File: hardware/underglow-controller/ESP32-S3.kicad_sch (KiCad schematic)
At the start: 38 parts, among them J101 CONSOLE, SW101 SW_Push, SW102 SW_Push, U101 ESP32-S3R2, U102 W25Q128JVS, Y101 40MHZ

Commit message: Hardware updates, firmware updates blah blah blah
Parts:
- added C111: 1uF, Capacitor_SMD:C_0402_1005Metric, symbol Device:C_Small
- added C118: 0.1uF, Capacitor_SMD:C_0402_1005Metric, symbol Device:C_Small
- added L103: 2nH, Inductor_SMD:L_0402_1005Metric, symbol Device:L_Small
- C108: value 1uF -> 10nf; MPN CGA2B1X7T0G105M050BC -> (none)
- C109: value 10uF -> 1uF; MPN GRT21BC81A106KE01L -> (none)
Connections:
- net +3V3: now also L103.2; no longer C101.1, C106.1, C110.1, R105.1, U101.2 (VDD3P3), U101.20 (VDD3P3_RTC), U101.29 (VDD_SPI), U101.3 (VDD3P3), U102.8 (VCC)
- net GND: now also C111.2, C118.2
- new net VDD3V3: C118.1, L103.1, U101.2 (VDD3P3), U101.3 (VDD3P3)
- new net VDDRTC: C101.1, U101.20 (VDD3P3_RTC)
- new net VDDSPI: C106.1, C110.1, C111.1, R105.1, U101.29 (VDD_SPI), U102.8 (VCC)
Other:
- moved on the sheet: C101, C102, C103, C104, C105, C106, C107, C108, C109

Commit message: hardware updates
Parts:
- removed AE101: Antenna_Shield, RF_Antenna:Texas_SWRA117D_2.4GHz_Left, symbol Device:Antenna_Shield
- removed J101: CONSOLE, Connector_PinHeader_1.27mm:PinHeader_1x06_P1.27mm_Vertical, symbol Connector_Generic:Conn_01x06
- added ANT101: 47948-0001, ConeCodes:Molex-47948-0001-0-0-0, symbol ConeCodes:47948-0001
- added C119: 2pF, Capacitor_SMD:C_0402_1005Metric, symbol Device:C_Small
- added J101: TC2030-IDC-NL_ESP, Connector:Tag-Connect_TC2030-IDC-FP_2x03_P1.27mm_Vertical, symbol ConeCodes:TC2030-IDC-NL_ESP
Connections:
- net FSPICS1: now also J101.6 (IO0)
- net GND: now also C119.1, J101.4 (GND)
- net RF_ANT: now also C119.2
- net RF_ANT_CHIP: now reaches C116.2, L102.2
- net RF_ANT_CHIP: now also ANT101.2 (FEEDING_PAD)
- net CHIP_PU renamed EN
- net EN: now also J101.1 (EN)
- net U0RXD renamed RXD
- net RXD: now also J101.5 (RX)
- net U0TXD renamed TXD
- net TXD: now also J101.3 (TX)
- no-connect marks 3 -> 6
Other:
- moved on the sheet: C114, C115, C116, L101, L102, TP101, TP102, TP103, TP104

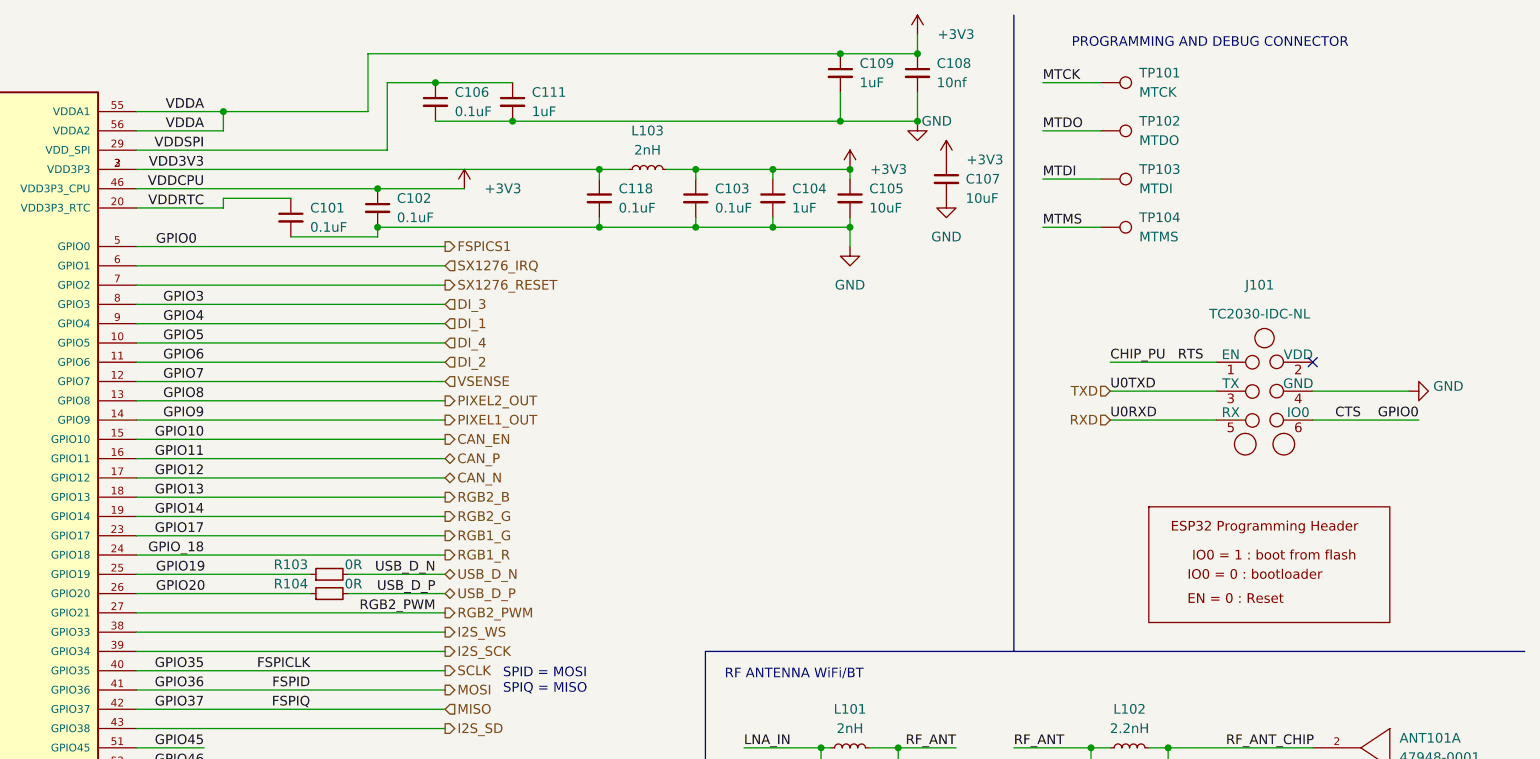
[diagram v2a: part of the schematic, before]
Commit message: more hardware updates. need to sort out the antenna for the radio  next
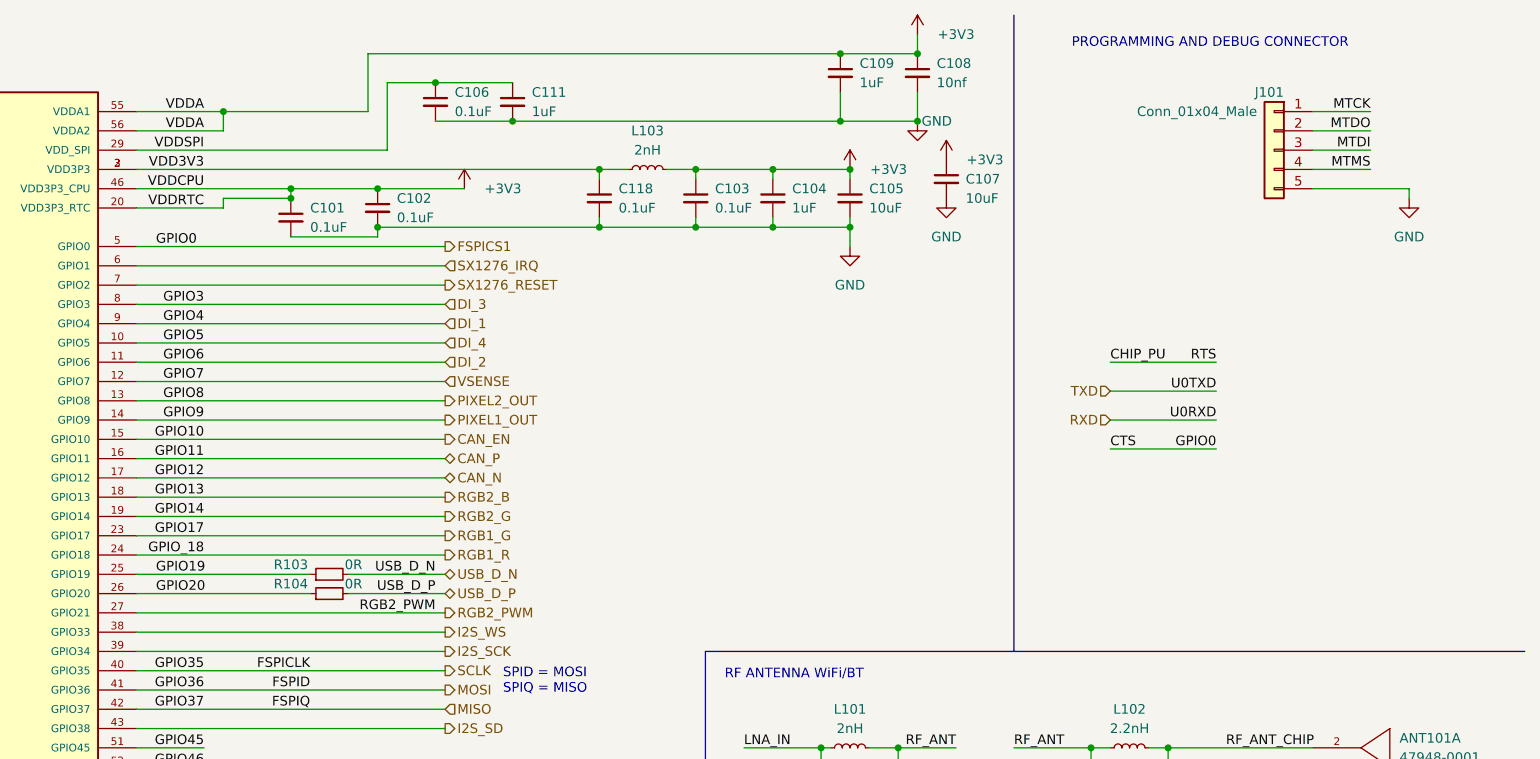
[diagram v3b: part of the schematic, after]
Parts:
- removed J101: TC2030-IDC-NL_ESP, Connector:Tag-Connect_TC2030-IDC-FP_2x03_P1.27mm_Vertical, symbol ConeCodes:TC2030-IDC-NL_ESP
- removed TP101: MTCK, TestPoint:TestPoint_Pad_D1.0mm, symbol Connector:TestPoint
- removed TP102: MTDO, TestPoint:TestPoint_Pad_D1.0mm, symbol Connector:TestPoint
- removed TP103: MTDI, TestPoint:TestPoint_Pad_D1.0mm, symbol Connector:TestPoint
- removed TP104: MTMS, TestPoint:TestPoint_Pad_D1.0mm, symbol Connector:TestPoint
- added J101: Conn_01x04_Male, Connector_PinHeader_2.54mm:PinHeader_1x05_P2.54mm_Vertical, symbol Connector_Generic:Conn_01x05
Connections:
- net VDDRTC is gone; now on net +3V3: C101.1, U101.20 (VDD3P3_RTC)
- net GND: now also J101.5 (Pin_5)
- net MTCK: now also J101.1 (Pin_1)
- net MTDI: now also J101.3 (Pin_3)
- net MTDO: now also J101.2 (Pin_2)
- net MTMS: now also J101.4 (Pin_4)
- no-connect marks 6 -> 5

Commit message: ughughughugh
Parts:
- added J102: UART, Connector:Tag-Connect_TC2030-IDC-FP_2x03_P1.27mm_Vertical, symbol Connector_Generic:Conn_02x03_Odd_Even
- J101: value Conn_01x04_Male -> JTAG; footprint Connector_PinHeader_2.54mm:PinHeader_1x05_P2.54mm_Vertical -> Connector:Tag-Connect_TC2050-IDC-FP_2x05_P1.27mm_Vertical; symbol Connector_Generic:Conn_01x05 -> Connector_Generic:Conn_02x05_Top_Bottom
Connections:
- net EN: now also J102.1 (Pin_1)
- net FSPICS1: now also J102.6 (Pin_6)
- net GND: now also J101.3 (Pin_3), J101.7 (Pin_7), J101.9 (Pin_9), J102.4 (Pin_4)
- net MTCK: now also J101.4 (Pin_4); no longer J101.1 (Pin_1)
- net MTDI: now also J101.8 (Pin_8); no longer J101.3 (Pin_3)
- net MTDO: now also J101.6 (Pin_6); no longer J101.2 (Pin_2)
- net MTMS: now also J101.2 (Pin_2); no longer J101.4 (Pin_4)
- net RXD: now also J102.5 (Pin_5)
- net TXD: now also J102.3 (Pin_3)
- net I2S_SCK renamed RGB2_CURRENT_SENSE
- net I2S_WS renamed RGB1_CURRENT_SENSE
- no-connect marks 5 -> 8

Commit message: hw updates pt 69 thousand
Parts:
- ANT101: digikey description ANTENNA 2.4GHZ 50 OHMS SMD -> (none)
- C108: value 10nf -> 0.1uF; MPN (none) -> CGA2B1X7R1C104M050BC
- C109: value 1uF -> 10uF; MPN (none) -> GRT21BC81A106KE01L
- C114: MPN TMK042CG4R6BD-W -> CBR04C469B5GAC
- J101: MPN (none) -> TC2050-IDC; now left out of the parts list
- J102: MPN TC2030-FTDI-C232HD-DDHSP-0-DTR -> TC2030-IDC; now left out of the parts list
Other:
- note added: "Should C109 and C107 be 1uF 0805?"
- moved on the sheet: C107

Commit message: hardware: prepare for production run
Signed-off-by: Connor Rigby <connorr@hey.com>
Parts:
- U101: LCSC C2913192 -> (none)
- U102: LCSC C113767 -> (none); now in the parts list
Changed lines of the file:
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@@
-      (effects (font (size 1.27 1.27)) (justify left) hide)
-    )
-    (property "digikey description" "" (id 4) (at 280.67 109.22 0)
       (effects (font (size 1.27 1.27)) (justify left) hide)
     )
@@
     )
     (pin "2")
+    (pin "1")
+    (pin "3")
+    (pin "4")
   )
   (symbol (lib_id "Device:C_Small") (at 205.74 21.59 0) (unit 1)
@@
       (effects (font (size 1.27 1.27)) (justify left) hide)
     )
-    (property "digikey description" "" (id 4) (at 252.73 147.32 0)
-      (effects (font (size 1.27 1.27)) (justify left) hide)
-    )
     (property "MPN" "WM4893CT-ND" (id 5) (at 252.73 149.86 0)
       (effects (font (size 1.27 1.27)) (justify left) hide)
@@
       (effects (font (size 1.27 1.27)) hide)
     )
+    (pin "2")
     (pin "1")
     (pin "3")
@@
     )
     (property "MPN" "ESP32-S3" (id 4) (at 77.47 20.32 0)
-      (effects (font (size 1.27 1.27)) hide)
-    )
-    (property "LCSC" "C2913192" (id 5) (at 77.47 71.12 0)
       (effects (font (size 1.27 1.27)) hide)
     )
@@
   )
   (symbol (lib_id "Memory_Flash:W25Q128JVS") (at 59.69 143.51 0) (unit 1)
-    (in_bom no) (on_board yes) (fields_autoplaced)
+    (in_bom yes) (on_board yes) (fields_autoplaced)
     (property "Reference" "U102" (id 0) (at 61.7094 130.81 0)
       (effects (font (size 1.27 1.27)) (justify left))
@@
       (effects (font (size 1.27 1.27)) hide)
     )
-    (property "LCSC" "C113767" (id 6) (at 59.69 143.51 0)
-      (effects (font (size 1.27 1.27)) hide)
-    )

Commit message: hardware: select some JLCPCB components
Signed-off-by: Connor Rigby <connorr@hey.com>
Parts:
- ANT101: Digikey (none) -> WM4893CT-ND; MPN WM4893CT-ND -> (none)
- C101, C102, C103, C106, C108, C110, C118: Digikey (none) -> CGA2B1X7R1C104M050BC; MPN CGA2B1X7R1C104M050BC -> (none)
- C104, C111, C117: Digikey (none) -> CGA2B1X7T0G105M050BC; MPN CGA2B1X7T0G105M050BC -> (none)
- C105, C107, C109: Digikey (none) -> GRT21BC81A106KE01L; MPN GRT21BC81A106KE01L -> (none)
- C112, C113: Digikey (none) -> GCM1555C1H160JA16D; MPN GCM1555C1H160JA16D -> (none)
- C114: Digikey (none) -> CBR04C469B5GAC; MPN CBR04C469B5GAC -> (none)
- C115: Digikey (none) -> UMK105UJ040CV-F; MPN UMK105UJ040CV-F -> (none)
- C116, C119: Digikey (none) -> UMK105CK020CVHF; MPN UMK105CK020CVHF -> (none)
- J101: Digikey (none) -> TC2050-IDC; MPN TC2050-IDC -> (none)
- J102: Digikey (none) -> TC2030-IDC; MPN TC2030-IDC -> (none)
- L101, L103: Digikey (none) -> LQG15HN2N0C02D; MPN LQG15HN2N0C02D -> (none)
- L102: Digikey (none) -> L-07C2N2SV6T; MPN L-07C2N2SV6T -> (none)
- R101, R106, R107, R108, R109: Digikey (none) -> RMCF0402JT10K0; MPN RMCF0402JT10K0 -> (none)
- R102: Digikey (none) -> RMCF0402FT499R; MPN RMCF0402FT499R -> (none)
- R103, R104: Digikey (none) -> RC0402JR-070RP; MPN RC0402JR-070RP -> (none)
- R105: Digikey (none) -> RNCF0402DTE100K; MPN RNCF0402DTE100K -> (none)
- SW101, SW102: Digikey (none) -> RS032G05A3SMRT; MPN RS032G05A3SMRT -> (none)
- U101: Digikey (none) -> ESP32-S3; MPN ESP32-S3 -> (none)
- U102: Digikey (none) -> W25Q128JVS; MPN W25Q128JVS -> (none)
- Y101: Digikey (none) -> ECS-400-10-37B2-CKY-TR; MPN ECS-400-10-37B2-CKY-TR -> (none)
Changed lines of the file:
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@@
       (effects (font (size 1.27 1.27)) hide)
     )
-    (property "MPN" "CGA2B1X7R1C104M050BC" (id 5) (at 163.83 36.83 0)
+    (property "Digikey" "CGA2B1X7R1C104M050BC" (id 5) (at 163.83 36.83 0)
       (effects (font (size 1.27 1.27)) hide)
     )
@@
       (effects (font (size 1.27 1.27)) (justify left) hide)
     )
-    (property "MPN" "WM4893CT-ND" (id 5) (at 283.21 109.22 0)
+    (property "Digikey" "WM4893CT-ND" (id 5) (at 283.21 109.22 0)
       (effects (font (size 1.27 1.27)) (justify left) hide)
     )
@@
       (effects (font (size 1.27 1.27)) hide)
     )
-    (property "MPN" "CGA2B1X7R1C104M050BC" (id 5) (at 205.74 21.59 0)
+    (property "Digikey" "CGA2B1X7R1C104M050BC" (id 5) (at 205.74 21.59 0)
       (effects (font (size 1.27 1.27)) hide)
     )
@@
       (effects (font (size 1.27 1.27)) (justify left) hide)
     )
-    (property "MPN" "WM4893CT-ND" (id 5) (at 252.73 149.86 0)
+    (property "Digikey" "WM4893CT-ND" (id 5) (at 252.73 149.86 0)
       (effects (font (size 1.27 1.27)) (justify left) hide)
     )
@@
       (effects (font (size 1.27 1.27)) hide)
     )
-    (property "MPN" "CGA2B1X7R1C104M050BC" (id 5) (at 134.62 38.1 0)
+    (property "Digikey" "CGA2B1X7R1C104M050BC" (id 5) (at 134.62 38.1 0)
       (effects (font (size 1.27 1.27)) hide)
     )
@@
       (effects (font (size 1.27 1.27)) hide)
     )
-    (property "MPN" "RC0402JR-070RP" (id 5) (at 128.27 88.9 0)
+    (property "Digikey" "RC0402JR-070RP" (id 5) (at 128.27 88.9 0)
       (effects (font (size 1.27 1.27)) hide)
     )
@@
       (effects (font (size 1.27 1.27)) hide)
     )
-    (property "MPN" "CGA2B1X7T0G105M050BC" (id 5) (at 125.73 143.51 0)
+    (property "Digikey" "CGA2B1X7T0G105M050BC" (id 5) (at 125.73 143.51 0)
       (effects (font (size 1.27 1.27)) hide)
     )
@@
       (effects (font (size 1.27 1.27)) hide)
     )
-    (property "MPN" "RMCF0402JT10K0" (id 5) (at 120.65 191.77 0)
+    (property "Digikey" "RMCF0402JT10K0" (id 5) (at 120.65 191.77 0)
       (effects (font (size 1.27 1.27)) hide)
     )
@@
       (effects (font (size 1.27 1.27)) hide)
     )
-    (property "MPN" "CGA2B1X7R1C104M050BC" (id 5) (at 31.75 132.08 0)
+    (property "Digikey" "CGA2B1X7R1C104M050BC" (id 5) (at 31.75 132.08 0)
       (effects (font (size 1.27 1.27)) hide)
     )
@@
       (effects (font (size 1.27 1.27)) hide)
     )
-    (property "MPN" "L-07C2N2SV6T" (id 5) (at 233.68 109.22 0)
+    (property "Digikey" "L-07C2N2SV6T" (id 5) (at 233.68 109.22 0)
       (effects (font (size 1.27 1.27)) hide)
     )
@@
       (effects (font (size 1.27 1.27)) hide)
     )
-    (property "MPN" "RMCF0402JT10K0" (id 5) (at 120.65 165.1 0)
+    (property "Digikey" "RMCF0402JT10K0" (id 5) (at 120.65 165.1 0)
       (effects (font (size 1.27 1.27)) hide)
     )
@@
       (effects (font (size 1.27 1.27)) hide)
     )
-    (property "MPN" "RNCF0402DTE100K" (id 5) (at 44.45 132.08 0)
+    (property "Digikey" "RNCF0402DTE100K" (id 5) (at 44.45 132.08 0)
       (effects (font (size 1.27 1.27)) hide)
     )
@@
       (effects (font (size 1.27 1.27)) hide)
     )
-    (property "MPN" "CGA2B1X7T0G105M050BC" (id 5) (at 186.69 36.83 0)
+    (property "Digikey" "CGA2B1X7T0G105M050BC" (id 5) (at 186.69 36.83 0)
       (effects (font (size 1.27 1.27)) hide)
     )
@@
       (effects (font (size 1.27 1.27)) hide)
     )
-    (property "MPN" "ECS-400-10-37B2-CKY-TR" (id 4) (at 41.91 175.26 0)
+    (property "Digikey" "ECS-400-10-37B2-CKY-TR" (id 4) (at 41.91 175.26 0)
       (effects (font (size 1.27 1.27)) hide)
     )
@@
       (effects (font (size 1.27 1.27)) (justify left bottom) hide)
     )
-    (property "MPN" "ESP32-S3" (id 4) (at 77.47 20.32 0)
+    (property "Digikey" "ESP32-S3" (id 4) (at 77.47 20.32 0)
       (effects (font (size 1.27 1.27)) hide)
     )
@@
       (effects (font (size 1.27 1.27)) hide)
     )
-    (property "MPN" "LQG15HN2N0C02D" (id 5) (at 196.85 109.22 0)
+    (property "Digikey" "LQG15HN2N0C02D" (id 5) (at 196.85 109.22 0)
       (effects (font (size 1.27 1.27)) hide)
     )
@@
       (effects (font (size 1.27 1.27)) hide)
     )
-    (property "MPN" "RMCF0402JT10K0" (id 5) (at 120.65 180.34 0)
+    (property "Digikey" "RMCF0402JT10K0" (id 5) (at 120.65 180.34 0)
       (effects (font (size 1.27 1.27)) hide)
     )
@@
       (effects (font (size 1.27 1.27)) hide)
     )
-    (property "MPN" "LQG15HN2N0C02D" (id 5) (at 170.18 33.02 0)
+    (property "Digikey" "LQG15HN2N0C02D" (id 5) (at 170.18 33.02 0)
       (effects (font (size 1.27 1.27)) hide)
     )
@@
       (effects (font (size 1.27 1.27)) hide)
     )
-    (property "MPN" "RMCF0402JT10K0" (id 5) (at 125.73 135.89 0)
+    (property "Digikey" "RMCF0402JT10K0" (id 5) (at 125.73 135.89 0)
       (effects (font (size 1.27 1.27)) hide)
     )
@@
       (effects (font (size 1.27 1.27)) hide)
     )
-    (property "MPN" "TC2050-IDC" (id 4) (at 234.95 33.02 0)
+    (property "Digikey" "TC2050-IDC" (id 4) (at 234.95 33.02 0)
       (effects (font (size 1.27 1.27)) hide)
     )
@@
       (effects (font (size 1.27 1.27)) hide)
     )
-    (property "MPN" "GRT21BC81A106KE01L" (id 7) (at 209.55 36.83 0)
+    (property "Digikey" "GRT21BC81A106KE01L" (id 7) (at 209.55 36.83 0)
       (effects (font (size 1.27 1.27)) hide)
     )
@@
       (effects (font (size 1.27 1.27)) hide)
     )
-    (property "MPN" "UMK105UJ040CV-F" (id 5) (at 203.2 114.3 0)
+    (property "Digikey" "UMK105UJ040CV-F" (id 5) (at 203.2 114.3 0)
       (effects (font (size 1.27 1.27)) hide)
     )
@@
       (effects (font (size 1.27 1.27)) hide)
     )
-    (property "MPN" "TC2030-IDC" (id 4) (at 227.33 62.23 0)
+    (property "Digikey" "TC2030-IDC" (id 4) (at 227.33 62.23 0)
       (effects (font (size 1.27 1.27)) hide)
     )
@@
       (effects (font (size 1.27 1.27)) hide)
     )
-    (property "MPN" "RS032G05A3SMRT " (id 5) (at 149.86 165.1 0)
+    (property "Digikey" "RS032G05A3SMRT " (id 5) (at 149.86 165.1 0)
       (effects (font (size 1.27 1.27)) hide)
     )
@@
       (effects (font (size 1.27 1.27)) hide)
     )
-    (property "MPN" "GCM1555C1H160JA16D" (id 5) (at 50.8 181.61 0)
+    (property "Digikey" "GCM1555C1H160JA16D" (id 5) (at 50.8 181.61 0)
       (effects (font (size 1.27 1.27)) hide)
     )
@@
       (effects (font (size 1.27 1.27)) hide)
     )
-    (property "MPN" "RMCF0402FT499R" (id 5) (at 45.72 83.82 0)
+    (property "Digikey" "RMCF0402FT499R" (id 5) (at 45.72 83.82 0)
       (effects (font (size 1.27 1.27)) hide)
     )
@@
       (effects (font (size 1.27 1.27)) hide)
     )
-    (property "MPN" "RMCF0402JT10K0" (id 5) (at 29.21 40.64 0)
+    (property "Digikey" "RMCF0402JT10K0" (id 5) (at 29.21 40.64 0)
       (effects (font (size 1.27 1.27)) hide)
     )
@@
       (effects (font (size 1.27 1.27)) hide)
     )
-    (property "MPN" "RS032G05A3SMRT " (id 5) (at 149.86 139.7 0)
+    (property "Digikey" "RS032G05A3SMRT " (id 5) (at 149.86 139.7 0)
       (effects (font (size 1.27 1.27)) hide)
     )
@@
       (effects (font (size 1.27 1.27)) hide)
     )
-    (property "MPN" "CGA2B1X7R1C104M050BC" (id 5) (at 123.19 39.37 0)
+    (property "Digikey" "CGA2B1X7R1C104M050BC" (id 5) (at 123.19 39.37 0)
       (effects (font (size 1.27 1.27)) hide)
     )
@@
       (effects (font (size 1.27 1.27)) hide)
     )
-    (property "MPN" "GRT21BC81A106KE01L" (id 7) (at 196.85 36.83 0)
+    (property "Digikey" "GRT21BC81A106KE01L" (id 7) (at 196.85 36.83 0)
       (effects (font (size 1.27 1.27)) hide)
     )
@@
       (effects (font (size 1.27 1.27)) hide)
     )
-    (property "MPN" "CGA2B1X7R1C104M050BC" (id 5) (at 176.53 36.83 0)
+    (property "Digikey" "CGA2B1X7R1C104M050BC" (id 5) (at 176.53 36.83 0)
       (effects (font (size 1.27 1.27)) hide)
     )
@@
       (effects (font (size 1.27 1.27)) hide)
     )
-    (property "MPN" "UMK105CK020CVHF" (id 5) (at 238.76 114.3 0)
+    (property "Digikey" "UMK105CK020CVHF" (id 5) (at 238.76 114.3 0)
       (effects (font (size 1.27 1.27)) hide)
     )
@@
       (effects (font (size 1.27 1.27)) hide)
     )
-    (property "MPN" "CGA2B1X7R1C104M050BC" (id 5) (at 142.24 24.13 0)
+    (property "Digikey" "CGA2B1X7R1C104M050BC" (id 5) (at 142.24 24.13 0)
       (effects (font (size 1.27 1.27)) hide)
     )
@@
       (effects (font (size 1.27 1.27)) hide)
     )
-    (property "MPN" "RC0402JR-070RP" (id 5) (at 128.27 86.36 0)
+    (property "Digikey" "RC0402JR-070RP" (id 5) (at 128.27 86.36 0)
       (effects (font (size 1.27 1.27)) hide)
     )
@@
       (effects (font (size 1.27 1.27)) hide)
     )
-    (property "MPN" "W25Q128JVS" (id 4) (at 59.69 143.51 0)
+    (property "Digikey" "W25Q128JVS" (id 4) (at 59.69 143.51 0)
       (effects (font (size 1.27 1.27)) hide)
     )
@@
       (effects (font (size 1.27 1.27)) hide)
     )
-    (property "MPN" "GRT21BC81A106KE01L" (id 7) (at 195.58 21.59 0)
+    (property "Digikey" "GRT21BC81A106KE01L" (id 7) (at 195.58 21.59 0)
       (effects (font (size 1.27 1.27)) hide)
     )
@@
       (effects (font (size 1.27 1.27)) hide)
     )
-    (property "MPN" "UMK105CK020CVHF" (id 5) (at 228.6 114.3 0)
+    (property "Digikey" "UMK105CK020CVHF" (id 5) (at 228.6 114.3 0)
       (effects (font (size 1.27 1.27)) hide)
     )
@@
       (effects (font (size 1.27 1.27)) hide)
     )
-    (property "MPN" "CGA2B1X7T0G105M050BC" (id 5) (at 152.4 24.13 0)
+    (property "Digikey" "CGA2B1X7T0G105M050BC" (id 5) (at 152.4 24.13 0)
       (effects (font (size 1.27 1.27)) hide)
     )
@@
       (effects (font (size 1.27 1.27)) hide)
     )
-    (property "MPN" "CBR04C469B5GAC" (id 5) (at 193.04 114.3 0)
+    (property "Digikey" "CBR04C469B5GAC" (id 5) (at 193.04 114.3 0)
       (effects (font (size 1.27 1.27)) hide)
     )
@@
       (effects (font (size 1.27 1.27)) hide)
     )
-    (property "MPN" "GCM1555C1H160JA16D" (id 5) (at 30.48 181.61 0)
-      (effects (font (size 1.27 1.27)) hide)
-    )
+    (property "Digikey" "GCM1555C1H160JA16D" (id 5) (at 30.48 181.61 0)
+      (effects (font (size 1.27 1.27)) hide)
+    )

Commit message: hardware: assign more JLC parts
Signed-off-by: Connor Rigby <connorr@hey.com>
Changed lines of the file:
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@@
     (effects (font (size 1.27 1.27)) (justify left bottom))
   )
-  (text "Should C109 and C107 be 1uF 0805?" (at 187.96 30.48 0)
+  (text "Should C109 and C107 be 1uF 0805?" (at 165.1 20.32 0)
     (effects (font (size 1 1)) (justify left bottom))
   )
